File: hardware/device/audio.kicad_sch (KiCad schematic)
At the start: 27 parts, among them J10 HP_OUT, J5 AUDIO_EXP, J8 LINE_OUT, J9 LINE_IN, U24 MIC, U29 NAU88C22YG

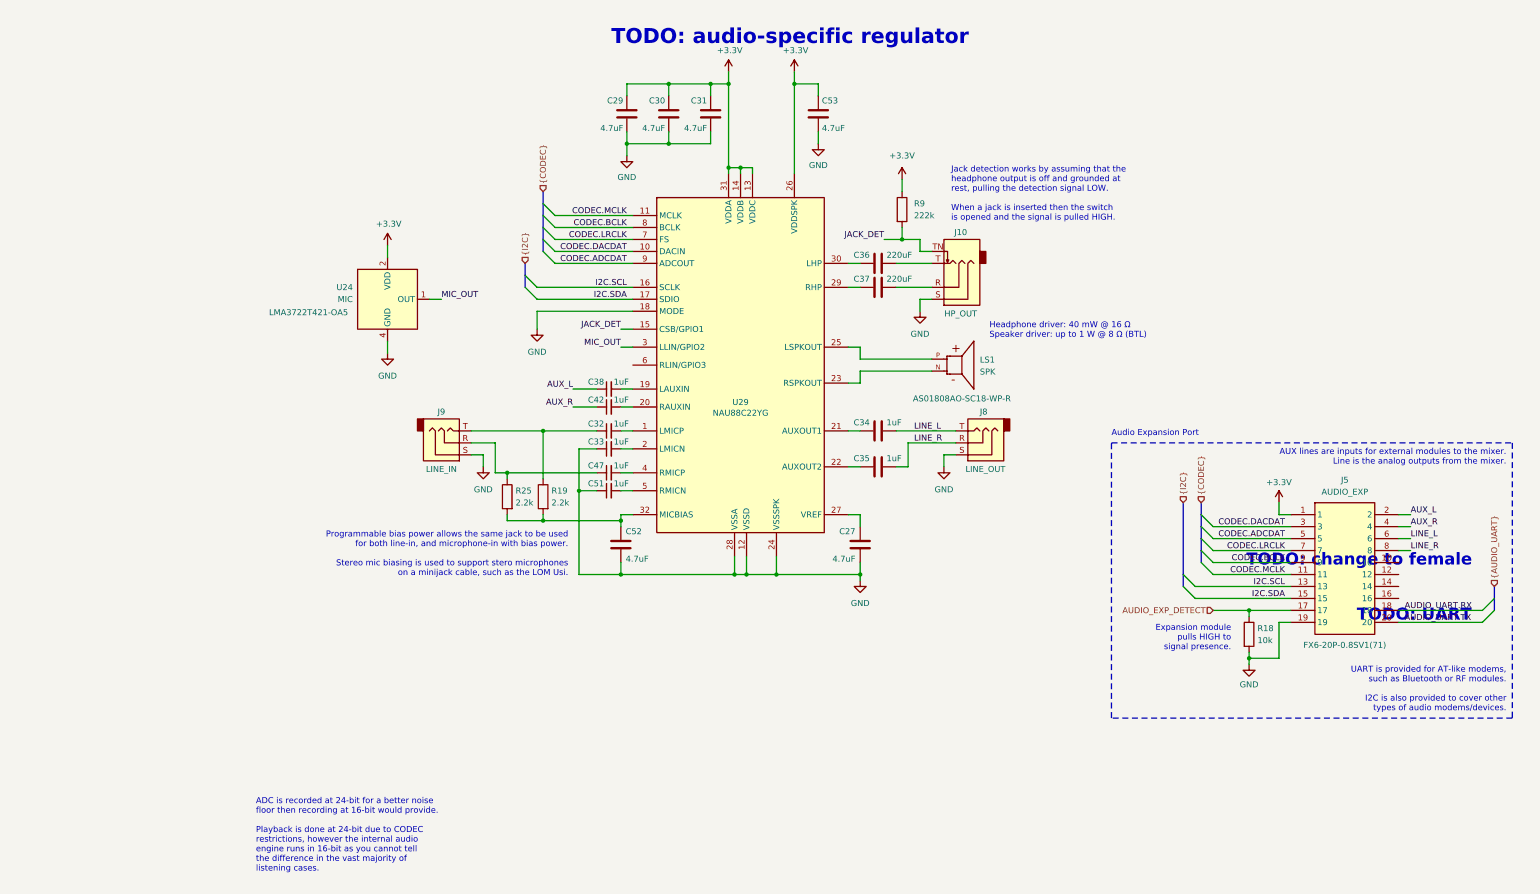
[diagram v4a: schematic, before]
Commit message: feat: add audio routing muxes
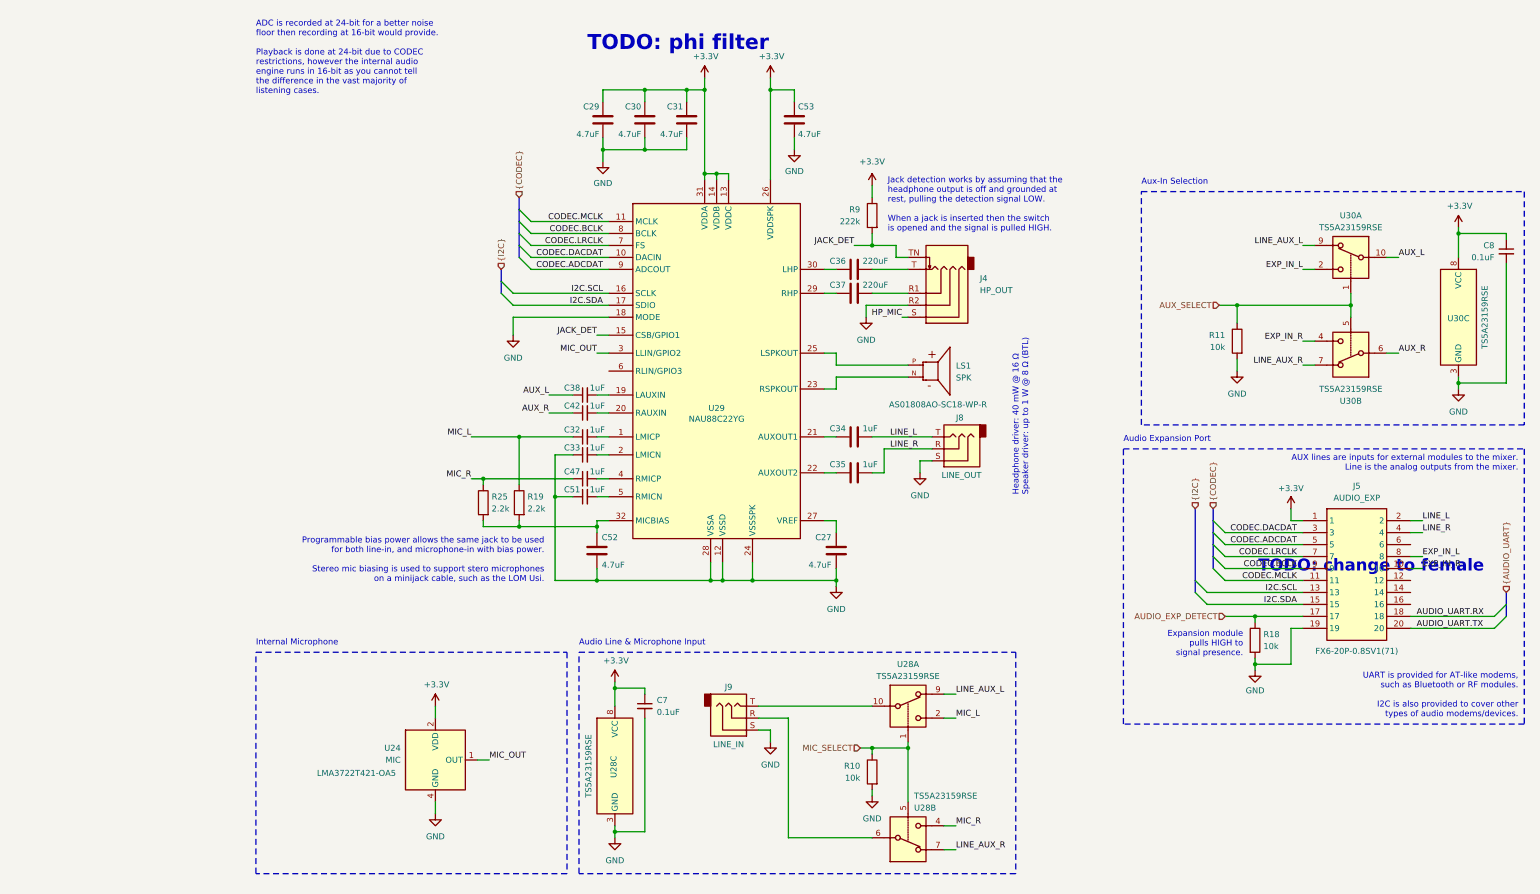
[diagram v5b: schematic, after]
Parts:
- removed J10: HP_OUT, Connector_Audio:Jack_3.5mm_CUI_SJ-3524-SMT_Horizontal, symbol Connector_Audio:AudioJack3_SwitchT
- added C7, C8: 0.1uF, symbol Device:C_Small
- added J4: HP_OUT, symbol Connector_Audio:AudioJack4_SwitchT1
- added R10, R11: 10k, Resistor_SMD:R_0201_0603Metric, symbol Device:R
- added U28, U30: TS5A23159RSE, Package_DFN_QFN:Texas_R-PUQFN-N10, symbol Analog_Switch:TS5A23159RSE
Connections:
- net +3.3V: now also C7.1, C8.1, U28.8 (VCC), U30.8 (VCC)
- net AUX_L: now also U30.10; no longer J5.2
- net AUX_R: now also U30.6; no longer J5.4
- net GND: now also C7.2, C8.2, J4.R2, R10.2, R11.2, U28.3 (GND), U30.3 (GND)
- net JACK_DET: now also J4.TN
- net LINE_L: now also J5.2; no longer J5.6
- net LINE_R: now also J5.4; no longer J5.8
- net MIC_R: now reaches C47.1, R25.1
- net MIC_R: now also U28.4; no longer J9.R
- net MIC_L: now reaches C32.1, R19.1
- net MIC_L: now also U28.2; no longer J9.T
- net at C37.2: now also J4.R1
- net EXP_IN_R: now reaches J5.10
- net EXP_IN_R: now also U30.4
- net at C36.2: now also J4.T
- new net: J9.R, U28.6
- new net: J9.T, U28.10
- new net AUX_SELECT: R11.1, U30.1, U30.5
- new net EXP_IN_L: J5.8, U30.2
- new net HP_MIC: J4.S
- new net LINE_AUX_L: U28.9, U30.9
- new net LINE_AUX_R: U28.7, U30.7
- new net MIC_SELECT: R10.1, U28.1, U28.5
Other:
- note added: "Audio Line & Microphone Input"
- note added: "Aux-In Selection"
- note added: "Internal Microphone"
- note added: "TODO: phi filter"
- note removed: "TODO: UART"
- note removed: "TODO: audio-specific regulator"
- moved on the sheet: C27, C29, C30, C31, C32, C33, C34, C35, C36, C37, C38, C42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

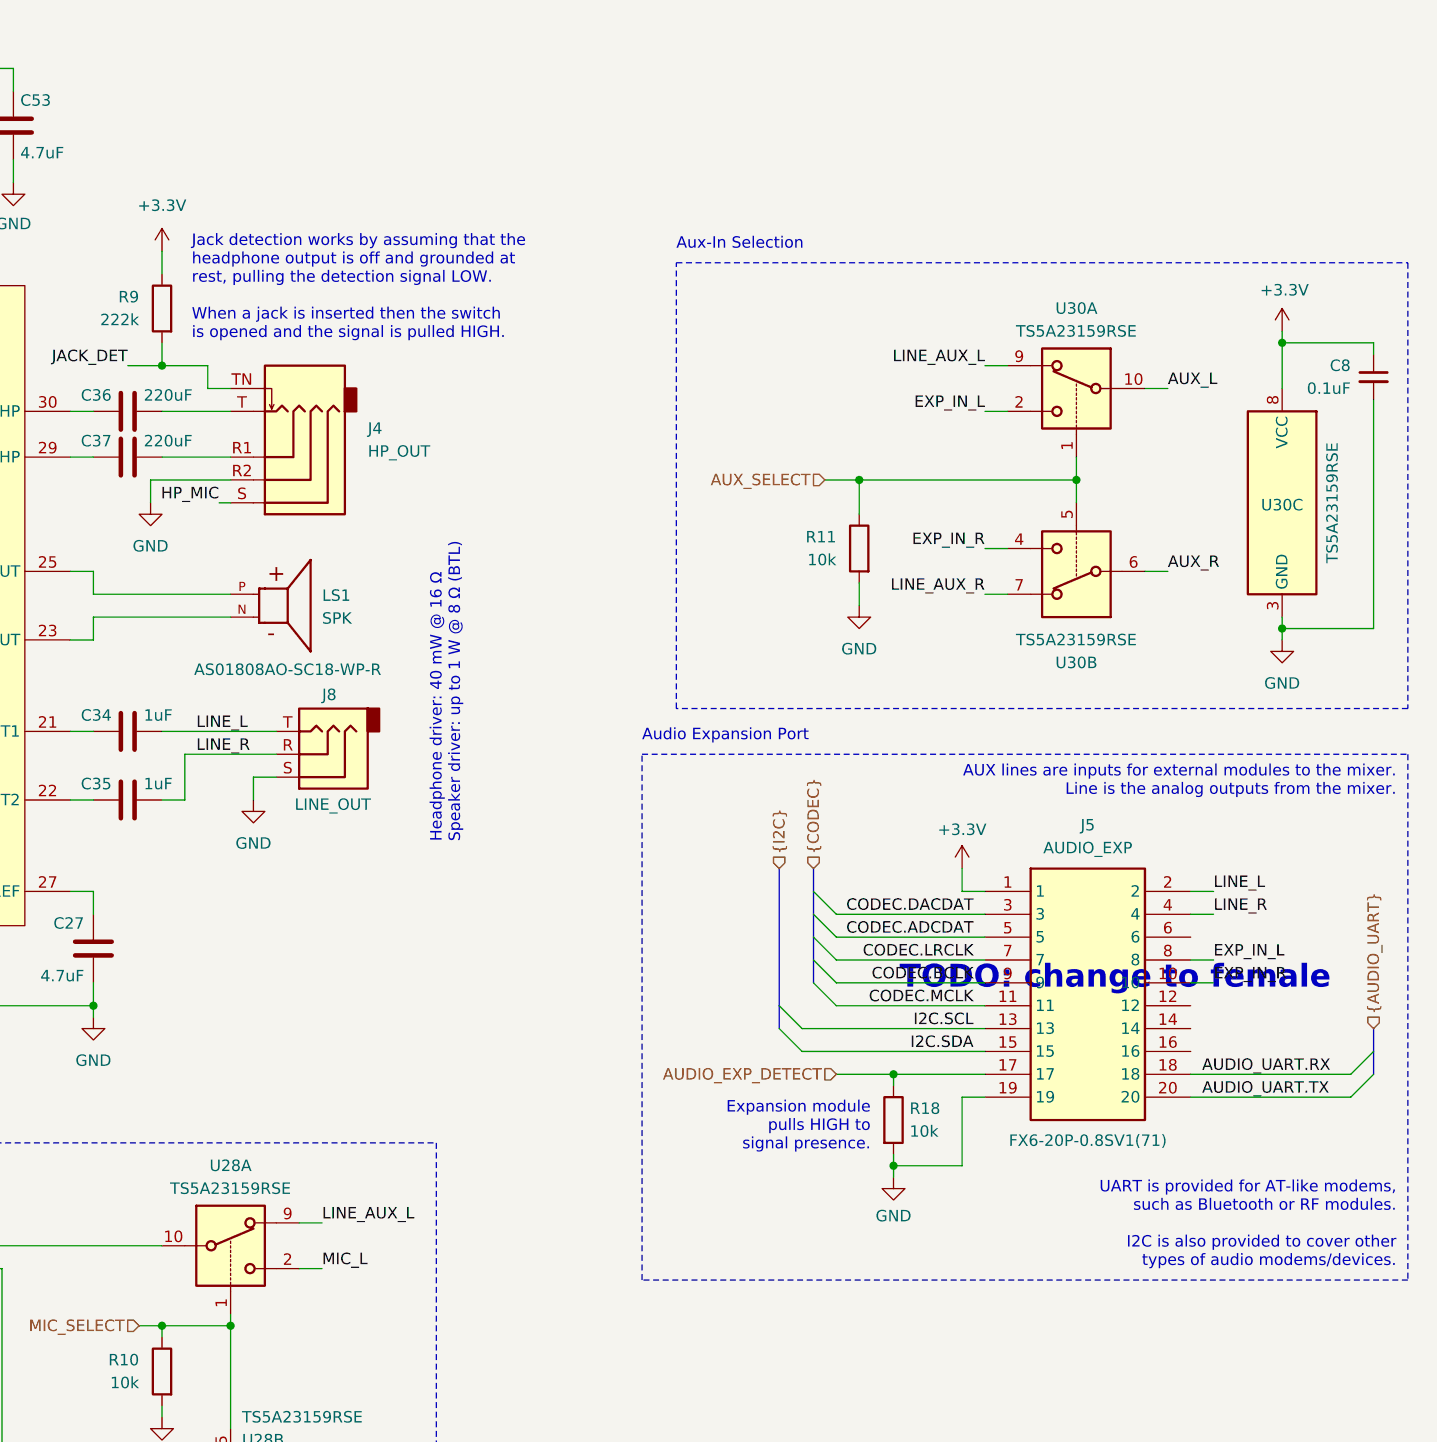
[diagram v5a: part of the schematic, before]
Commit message: feat: various layout, start adding capacitive pads
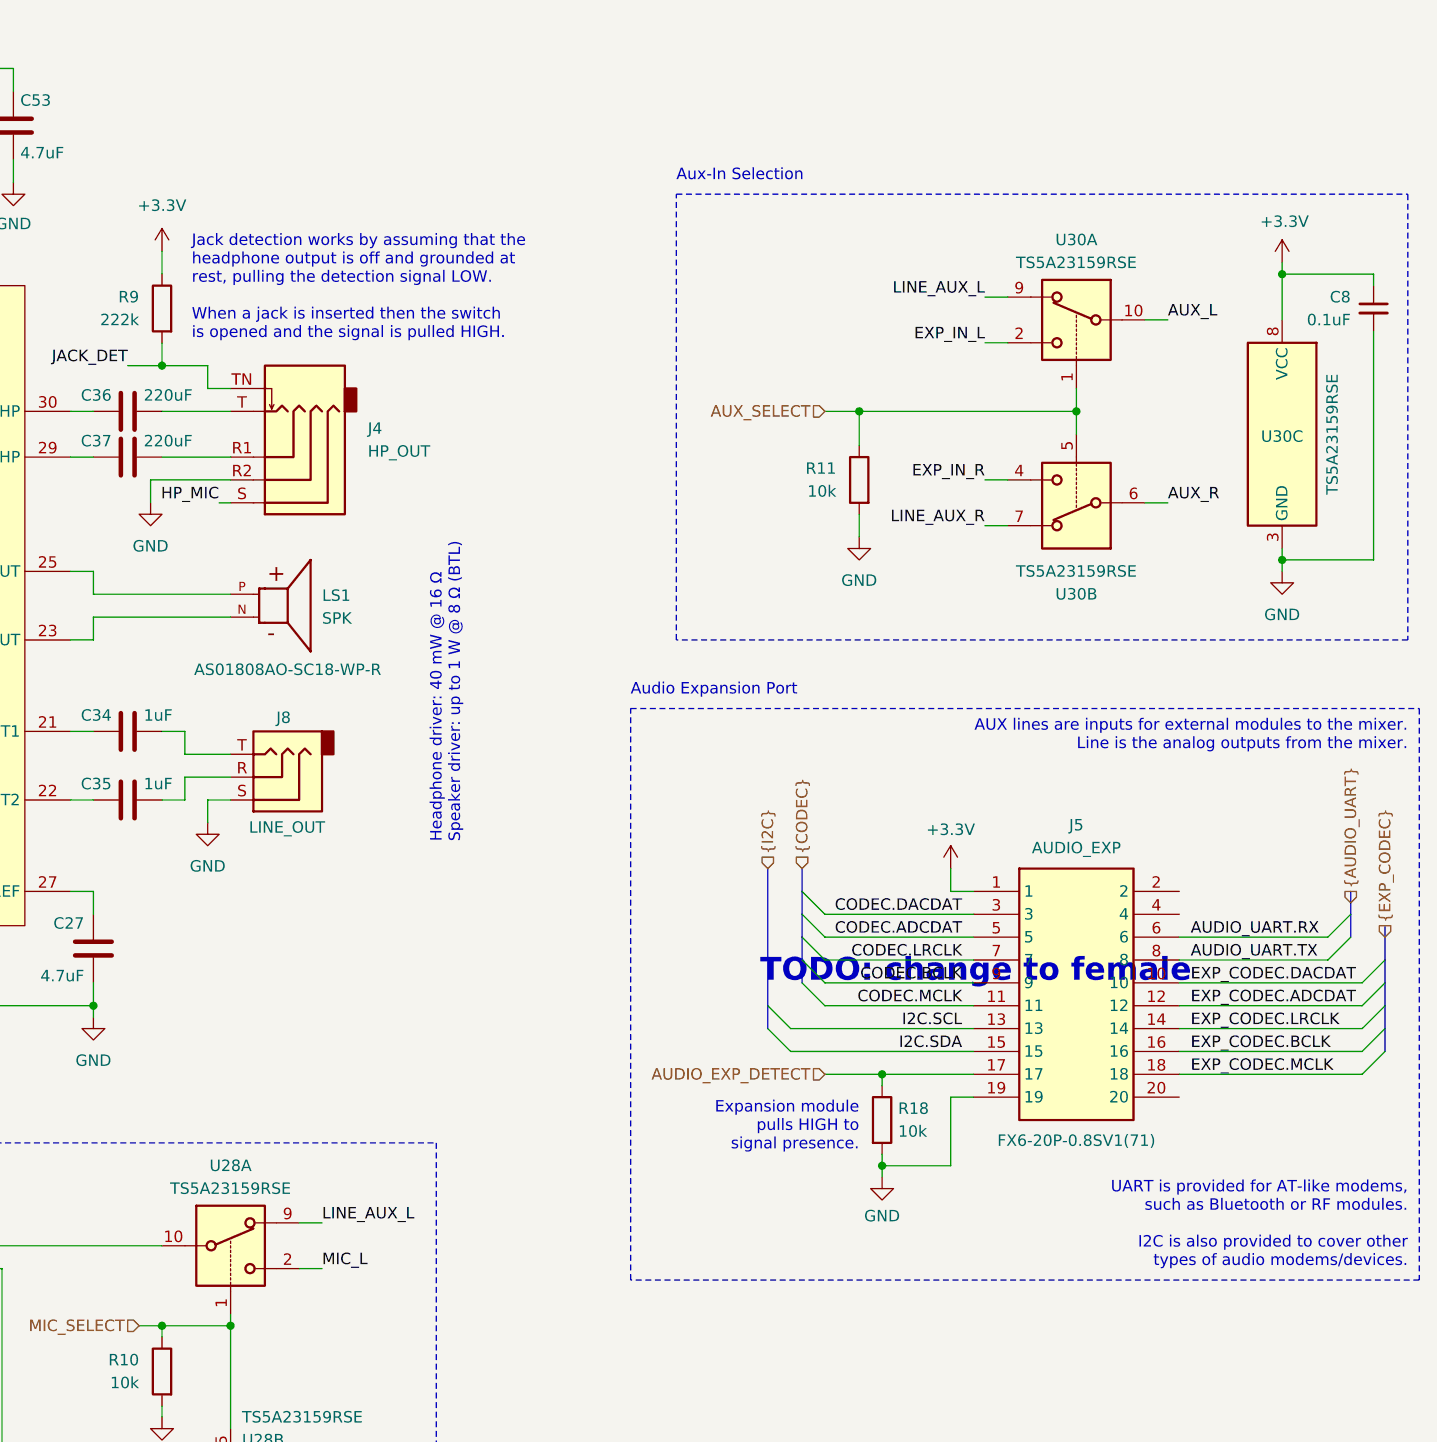
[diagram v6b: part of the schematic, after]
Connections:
- net AUDIO_UART.RX: now also J5.6; no longer J5.18
- net AUDIO_UART.TX: now also J5.8; no longer J5.20
- net EXP_IN_L: no longer J5.8
- net EXP_IN_R: no longer J5.10
- net EXP_CODEC.ADCDAT: now reaches J5.12
- net EXP_CODEC.LRCLK: now reaches J5.14
- net EXP_CODEC.BCLK: now reaches J5.16
- net LINE_L: no longer names the net of C34.2, J8.T
- net LINE_L: no longer J5.2
- net LINE_R: no longer names the net of C35.2, J8.R
- net LINE_R: no longer J5.4
- new net EXP_CODEC.DACDAT: J5.10
- new net EXP_CODEC.MCLK: J5.18
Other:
- moved on the sheet: C8, J5, J8, R11, R18, U30A, U30B, U30C

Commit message: chore: schematic organization
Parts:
- C7, C8: footprint (none) -> Capacitor_SMD:C_0201_0603Metric
- J8, J9: JLC (none) -> C4991872
- U24: JLC (none) -> C5373233
- U28, U30: JLC (none) -> C138710
- U29: JLC (none) -> C914209
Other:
- note added: "Analog MUX for switching line-in input modes"
- note added: "Audio ADC and DAC"
- note added: "Audio CODEC"
- note added: "Connector for audio expension modules"
- note added: "MEMs Microphone for internal recording input"
- moved on the sheet: C27, C29, C30, C31, C32, C33, C34, C35, C36, C37, C38, C42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

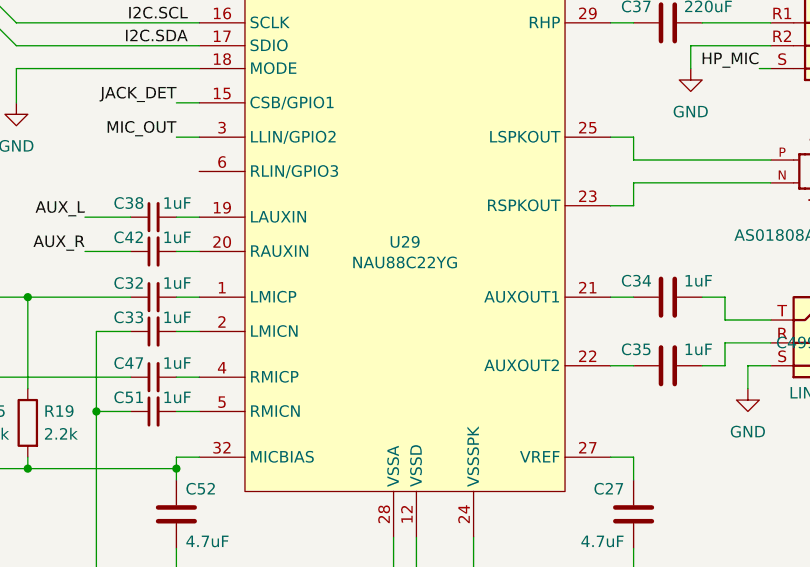
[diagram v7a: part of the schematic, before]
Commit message: feat: add plated mounting holes
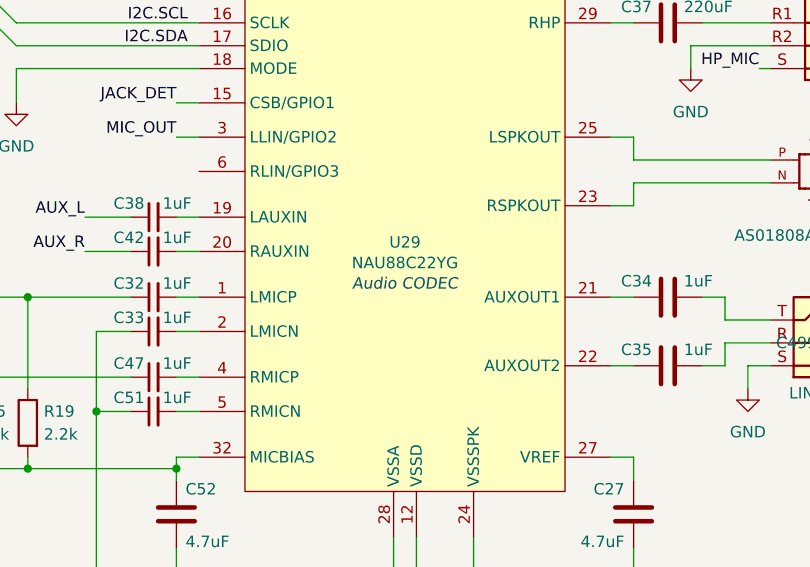
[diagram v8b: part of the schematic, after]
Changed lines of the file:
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@@
+		)
+	)
+	(text "Audio CODEC"
+		(exclude_from_sim no)
+		(at 88.9 98.298 0)
+		(effects
+			(font
+				(size 1.27 1.27)
+				(thickness 0.1588)
+				(italic yes)
+				(color 132 132 132 1)
+			)
+			(justify top)
 		)
 	)
